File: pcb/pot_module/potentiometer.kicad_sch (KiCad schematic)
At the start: 2 parts, among them J1 Conn_01x03

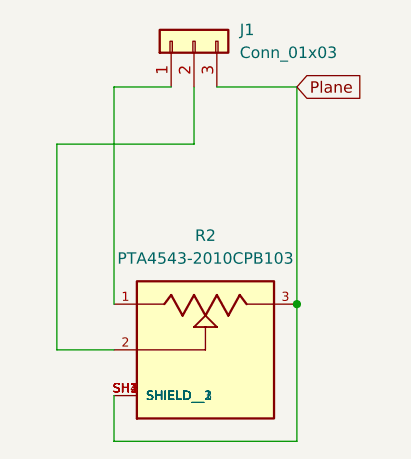
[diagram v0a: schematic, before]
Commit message: Tweak pot module
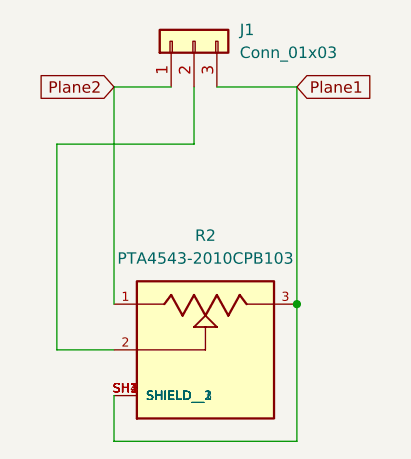
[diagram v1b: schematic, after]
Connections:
- net Plane2: now reaches J1.1 (Pin_1), R2.1
- net Plane renamed Plane1
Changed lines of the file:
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@@
 		)
 	)
-	(global_label "Plane"
+	(global_label "Plane1"
 		(shape input)
 		(at 143.51 90.17 0)
@@
 		)
 		(property "Intersheetrefs" "${INTERSHEET_REFS}"
-			(at 151.817 90.17 0)
+			(at 153.0265 90.17 0)
 			(hide yes)
 			(show_name no)
@@
 			)
 		)
+	)
+	(global_label "Plane2"
+		(shape input)
+		(at 123.19 90.17 180)
+		(fields_autoplaced yes)
+		(effects
+			(font
+				(size 1.27 1.27)
+			)
+			(justify right)
+		)
+		(property "Intersheetrefs" "${INTERSHEET_REFS}"
+			(at 113.6735 90.17 0)
+			(hide yes)
+			(show_name no)
+			(do_not_autoplace no)
+			(effects
+				(font
+					(size 1.27 1.27)
+				)
+				(justify right)
+			)
+		)
